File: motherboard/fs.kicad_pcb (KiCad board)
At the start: 4 copper layers, 177.8 x 114.3 mm, 229 parts, among them J101 Header, J102 640389-2, J201 BNC, J202 Conn_01x05, J203 BNC, J301 BNC, J302 BNC, J303 BNC, J304 BNC, J305 BNC, J306 BNC, Q101 MJD44H11, Q102 MJD45H11, Q201 2N7002, Q202 2N7002, Q203 2N7002, U101 INA132UA, U102 LM741C, U103 LMH6609, U104 LM317, U105 LM337, U106 LM340-5, U107 MC7905ACD2T, U201 LMH6609, U202 SYPD-1, U203 LM393, U204 AD797AR, U205 LM393, U206 OPA192IDR, U301 LMH6609, U302 LMH6609, U303 LMH6609, U304 LMH6609, U305 LMH6609, U306 LMH6609

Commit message: add testpoints
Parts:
- added TP101: TestPoint, TestPoint:TestPoint_THTPad_D2.0mm_Drill1.0mm, F.Cu at (163.2, 36.8)
- added TP102: TestPoint, TestPoint:TestPoint_THTPad_D2.0mm_Drill1.0mm, F.Cu at (43.8, 87.6)
- added TP103: TestPoint, TestPoint:TestPoint_THTPad_D2.0mm_Drill1.0mm, F.Cu at (73.7, 99.1)
- added TP104: TestPoint, TestPoint:TestPoint_THTPad_D2.0mm_Drill1.0mm, F.Cu at (95.2, 112.4)
- added TP105: TestPoint, TestPoint:TestPoint_THTPad_D2.0mm_Drill1.0mm, F.Cu at (114.9, 112.4)
- added TP106: TestPoint, TestPoint:TestPoint_THTPad_D2.0mm_Drill1.0mm, F.Cu at (158.8, 112.4)
- added TP107: TestPoint, TestPoint:TestPoint_THTPad_D2.0mm_Drill1.0mm, F.Cu at (204.5, 112.4)
- added TP108: TestPoint, TestPoint:TestPoint_THTPad_D2.0mm_Drill1.0mm, F.Cu at (138.4, 82.5)
- added TP109: TestPoint, TestPoint:TestPoint_THTPad_D2.0mm_Drill1.0mm, F.Cu at (202.6, 47.0)
- added TP110: TestPoint, TestPoint:TestPoint_THTPad_D2.0mm_Drill1.0mm, F.Cu at (43.8, 99.1)
- added TP111: TestPoint, TestPoint:TestPoint_THTPad_D2.0mm_Drill1.0mm, F.Cu at (64.8, 134.6)
- added TP112: TestPoint, TestPoint:TestPoint_THTPad_D1.0mm_Drill0.5mm, F.Cu at (124.5, 66.0)
- added TP113: TestPoint, TestPoint:TestPoint_THTPad_D1.0mm_Drill0.5mm, F.Cu at (118.7, 56.8)
- added TP114: TestPoint, TestPoint:TestPoint_THTPad_D1.0mm_Drill0.5mm, F.Cu at (126.4, 57.1)
- added TP115: TestPoint, TestPoint:TestPoint_THTPad_D1.0mm_Drill0.5mm, F.Cu at (120.7, 59.1)
- added TP116: TestPoint, TestPoint:TestPoint_THTPad_D1.0mm_Drill0.5mm, F.Cu at (117.5, 66.0)
- added TP117: TestPoint, TestPoint:TestPoint_THTPad_D1.0mm_Drill0.5mm, F.Cu at (117.5, 78.1)
- added TP118: TestPoint, TestPoint:TestPoint_THTPad_D1.0mm_Drill0.5mm, F.Cu at (121.3, 81.3)
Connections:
- J101 pad 8: /SCL10L_+5VREF -> /SC10L_+5VREF
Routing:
- net /VARAC_MON: track 0.00 -> 12.5 mm
- net /TEMP_CTL: track 0.00 -> 8.66 mm
- net /FREQ_CTL: track 5.12 -> 13.0 mm
- net /AGC_MON: track 0.00 -> 6.19 mm
- net /HEAT_MON: track 0.00 -> 5.44 mm
- net /AMPL_CTL: track 0.00 -> 5.06 mm
- net /SC10L_+5VREF: track 0.00 -> 3.28 mm

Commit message: update bead value for ocxo power
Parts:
- FB101: value 742863160 -> 9.5A BEAD
- R110: value 18R / 5W -> 18R 5W
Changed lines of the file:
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@@
 			)
 		)
-		(property "Value" "742863160"
+		(property "Value" "9.5A BEAD"
 			(at 0 0 0)
 			(unlocked yes)
@@
 			)
 		)
-		(property "Value" "18R / 5W"
+		(property "Value" "18R 5W"
 			(at 15.24 -5.62 180)
 			(layer "B.Fab")

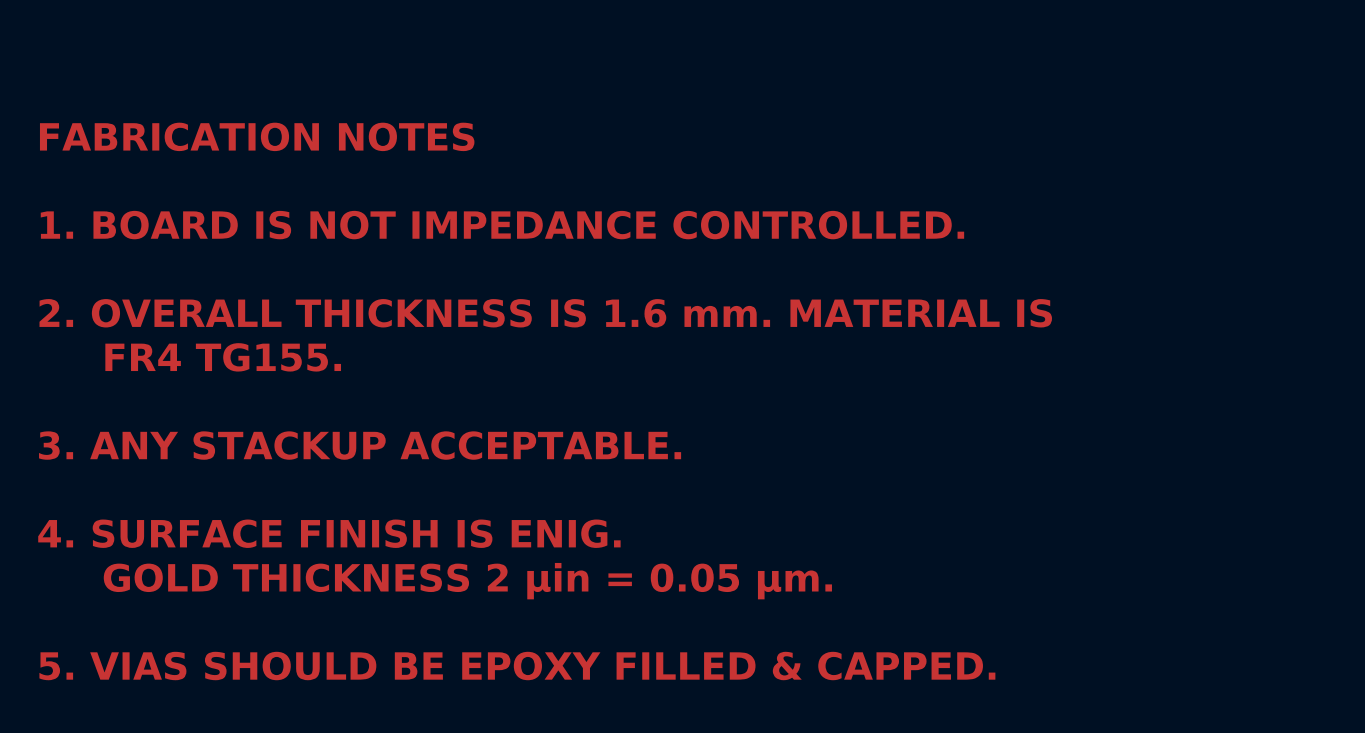
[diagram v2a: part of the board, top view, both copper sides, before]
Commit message: move fab notes to text file
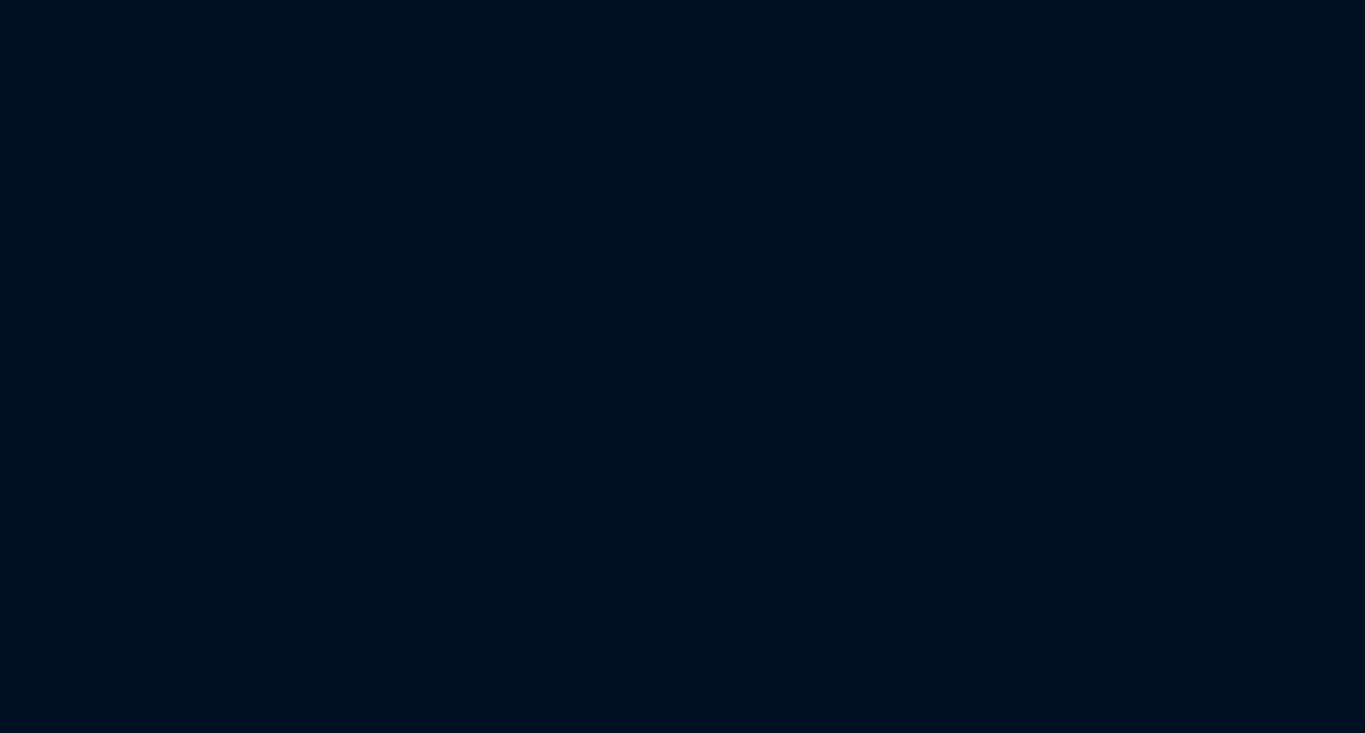
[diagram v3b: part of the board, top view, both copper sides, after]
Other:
- rule pad_to_mask_clearance: 0 -> 0.0508
- board text removed: "FABRICATION NOTES 1. BOARD IS NOT IMPEDANCE CONTROLLED. 2. OVERALL THICKNESS IS 1.6 mm. MATERIAL IS FR4 TG155. 3. ANY STACKUP ACCEPTABLE. 4. SURFACE FINISH IS ENIG. GOLD THICKNESS 2 μin = 0.05 μm. 5. VIAS SHOULD BE EPOXY FILLED & CAPPED."
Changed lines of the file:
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@@
 			(dielectric_constraints no)
 		)
-		(pad_to_mask_clearance 0)
+		(pad_to_mask_clearance 0.0508)
 		(allow_soldermask_bridges_in_footprints no)
 		(tenting
@@
 		(layer "Edge.Cuts")
 	)
-	(gr_text "FABRICATION NOTES\n\n1. BOARD IS NOT IMPEDANCE CONTROLLED.\n\n2. OVERALL THICKNESS IS 1.6 mm. MATERIAL IS\n     FR4 TG155.\n\n3. ANY STACKUP ACCEPTABLE.\n\n4. SURFACE FINISH IS ENIG.\n     GOLD THICKNESS 2 μin = 0.05 μm.\n\n5. VIAS SHOULD BE EPOXY FILLED & CAPPED."
-		(at 29.21 194.31 0)
-		(layer "F.Cu")
-		(effects
-			(font
-				(size 1.5 1.5)
-				(thickness 0.3)
-				(bold yes)
-			)
-			(justify left bottom)
-		)
-	)
 	(gr_text "FS720 / JK / JUL26 / REV A"
 		(at 163.449 105.537 0)
@@
 	)
 	(segment
+		(start 114.462 76.835)
+		(end 117.637 80.01)
+		(width 0.2)
+		(layer "F.Cu")
+		(net "/TEMP_CTL")
+	)
+	(segment
+		(start 117.637 80.01)
+		(end 120.015 80.01)
+		(width 0.2)
+		(layer "F.Cu")
+		(net "/TEMP_CTL")
+	)
+	(segment
+		(start 120.015 80.01)
+		(end 121.285 81.28)
+		(width 0.2)
+		(layer "F.Cu")
+		(net "/TEMP_CTL")
+	)
+	(segment
 		(start 175.838 62.149)
 		(end 175.838 60.625)
@@
 	)
 	(segment
+		(start 114.462 74.295)
+		(end 117.475 77.308)
+		(width 0.2)
+		(layer "F.Cu")
+		(net "/AMPL_CTL")
+	)
+	(segment
+		(start 117.475 77.308)
+		(end 117.475 78.105)
+		(width 0.2)
+		(layer "F.Cu")
+		(net "/AMPL_CTL")
+	)
+	(segment
 		(start 59.141529 97.409)
 		(end 65.532 103.799471)
@@
 	)
 	(segment
+		(start 117.267 56.78)
+		(end 114.462 53.975)
+		(width 0.2)
+		(layer "F.Cu")
+		(net "/HEAT_MON")
+	)
+	(segment
+		(start 118.745 56.78)
+		(end 117.267 56.78)
+		(width 0.2)
+		(layer "F.Cu")
+		(net "/HEAT_MON")
+	)
+	(segment
 		(start 95.078 127.5054)
 		(end 95.078 126.630401)
@@
 	)
 	(segment
-		(start 117.267 56.78)
-		(end 114.462 53.975)
-		(width 0.2)
-		(layer "F.Cu")
-		(net "/HEAT_MON")
-	)
-	(segment
-		(start 118.745 56.78)
-		(end 117.267 56.78)
-		(width 0.2)
-		(layer "F.Cu")
-		(net "/HEAT_MON")
-	)
-	(segment
 		(start 114.462 56.515)
 		(end 115.527 57.58)
@@
 	)
 	(segment
-		(start 114.462 74.295)
-		(end 117.475 77.308)
-		(width 0.2)
-		(layer "F.Cu")
-		(net "/AMPL_CTL")
-	)
-	(segment
-		(start 117.475 77.308)
-		(end 117.475 78.105)
-		(width 0.2)
-		(layer "F.Cu")
-		(net "/AMPL_CTL")
-	)
-	(segment
-		(start 114.462 76.835)
-		(end 117.637 80.01)
-		(width 0.2)
-		(layer "F.Cu")
-		(net "/TEMP_CTL")
-	)
-	(segment
-		(start 117.637 80.01)
-		(end 120.015 80.01)
-		(width 0.2)
-		(layer "F.Cu")
-		(net "/TEMP_CTL")
-	)
-	(segment
-		(start 120.015 80.01)
-		(end 121.285 81.28)
-		(width 0.2)
-		(layer "F.Cu")
-		(net "/TEMP_CTL")
-	)
-	(segment
